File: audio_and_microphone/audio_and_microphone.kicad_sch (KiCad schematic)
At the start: 14 parts, among them U6 ${SIM.PARAMS}

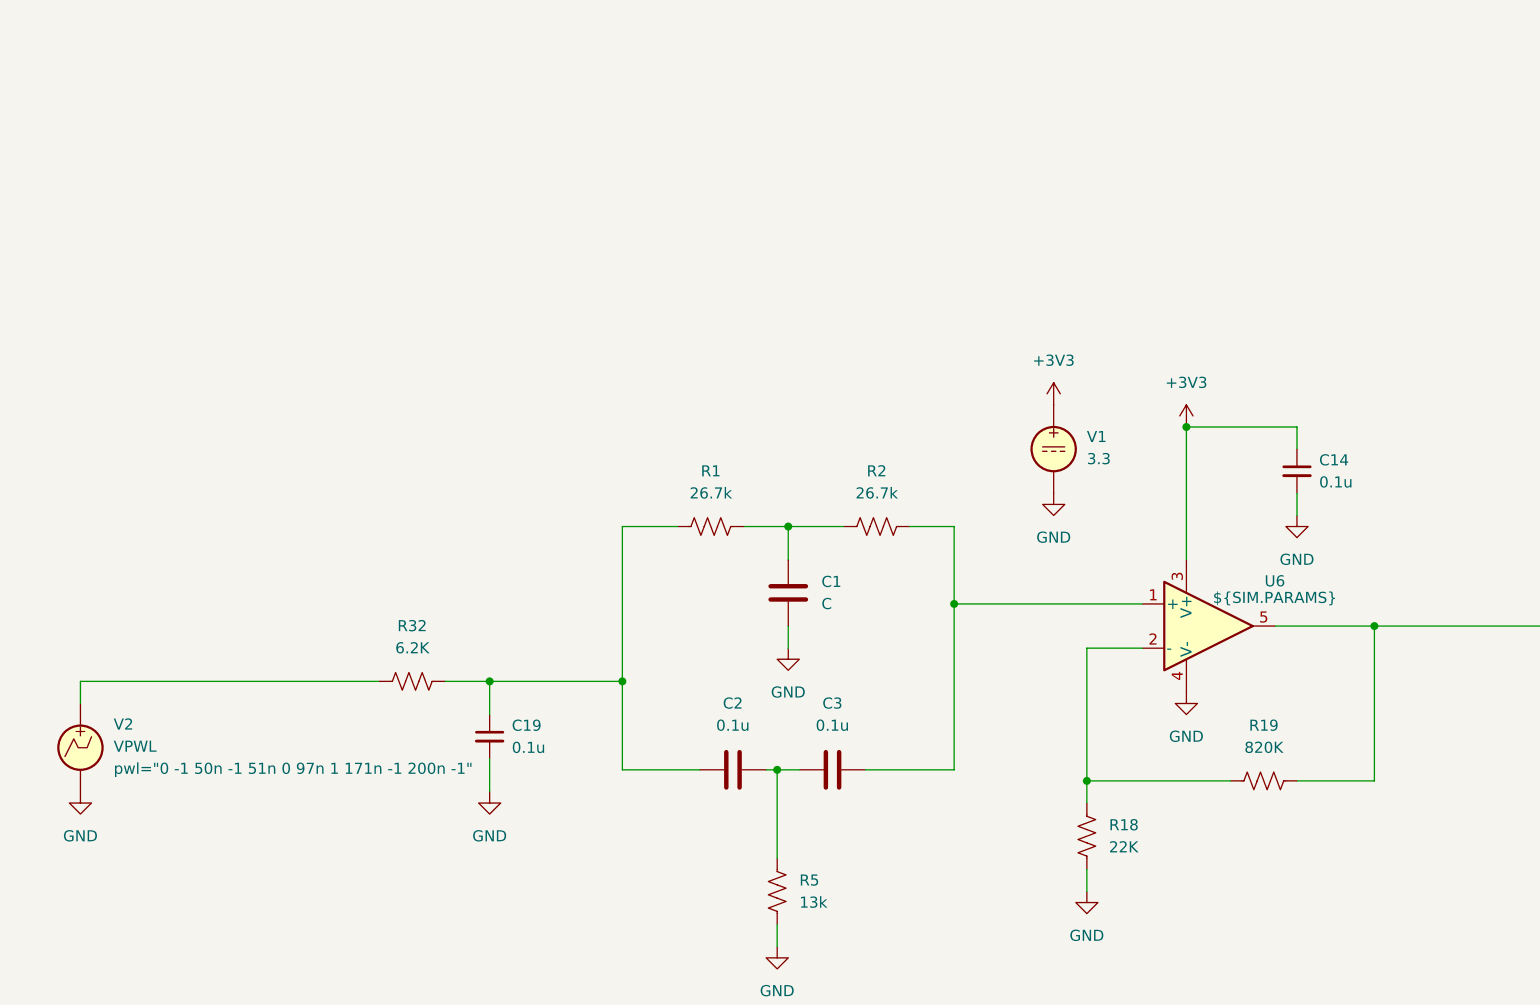
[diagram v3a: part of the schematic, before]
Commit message: pcb update with pin connectors
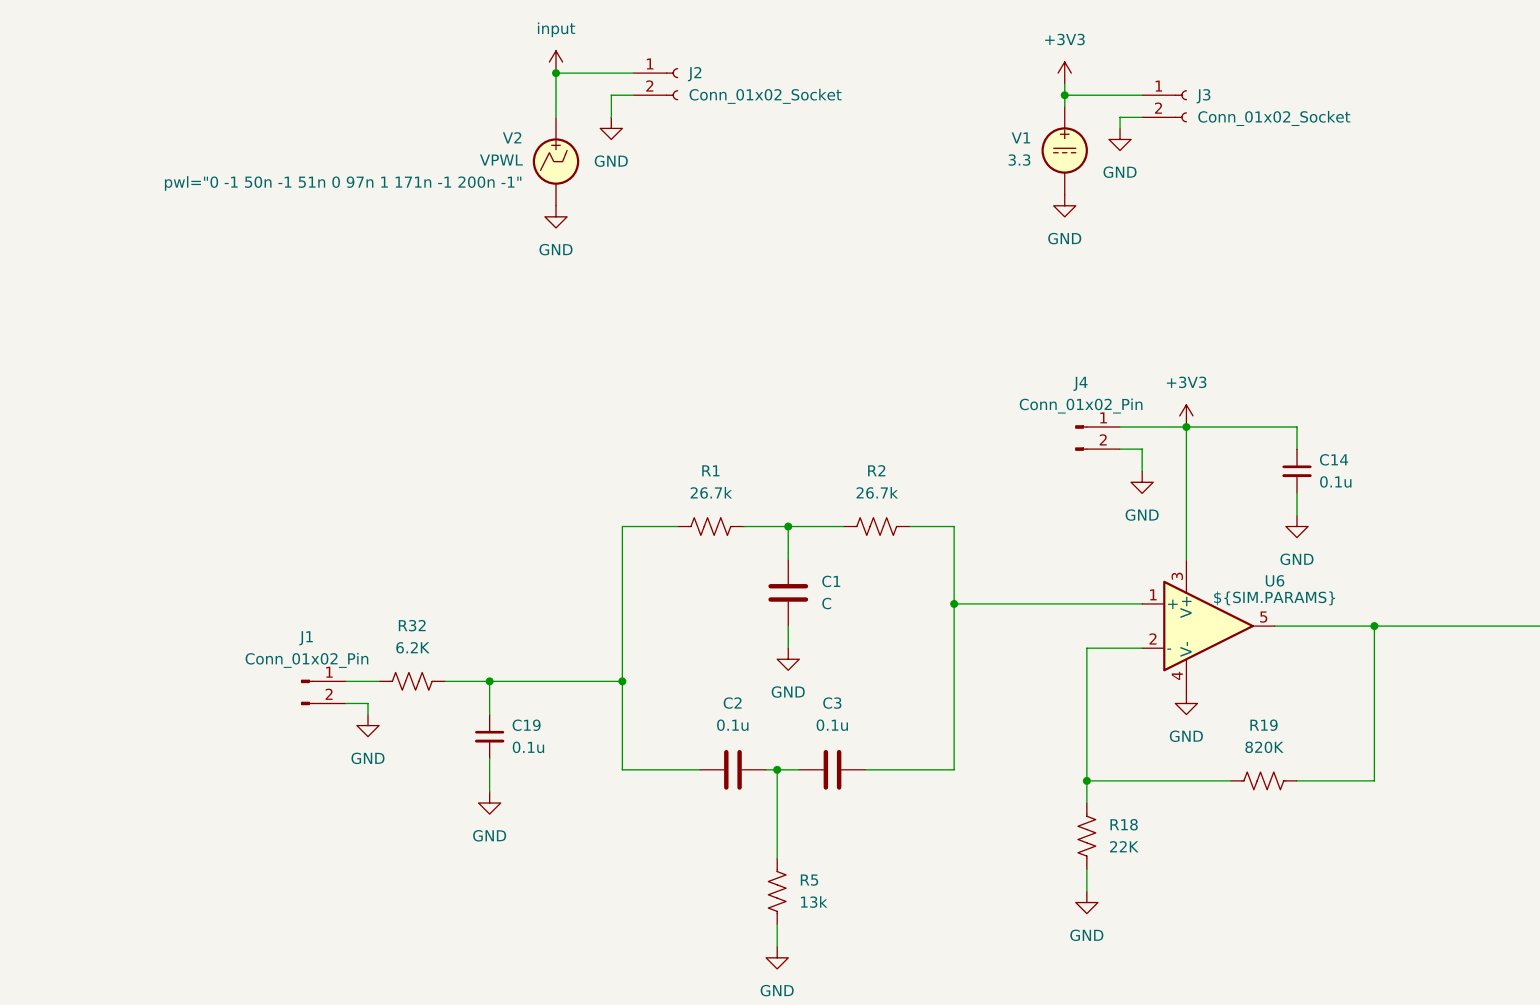
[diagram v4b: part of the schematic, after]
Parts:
- added J1, J4: Conn_01x02_Pin, Connector_JST:JST_XA_B02B-XASK-1-A_1x02_P2.50mm_Vertical, symbol Connector:Conn_01x02_Pin
- added J2, J3: Conn_01x02_Socket, symbol Connector:Conn_01x02_Socket
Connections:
- net +3V3: now also J3.1 (Pin_1), J4.1 (Pin_1)
- net GND: now also J1.2 (Pin_2), J2.2 (Pin_2), J3.2 (Pin_2), J4.2 (Pin_2)
- net at R32.2: now also J1.1 (Pin_1); no longer V2.1
- new net input: J2.1 (Pin_1), V2.1
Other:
- moved on the sheet: V1, V2

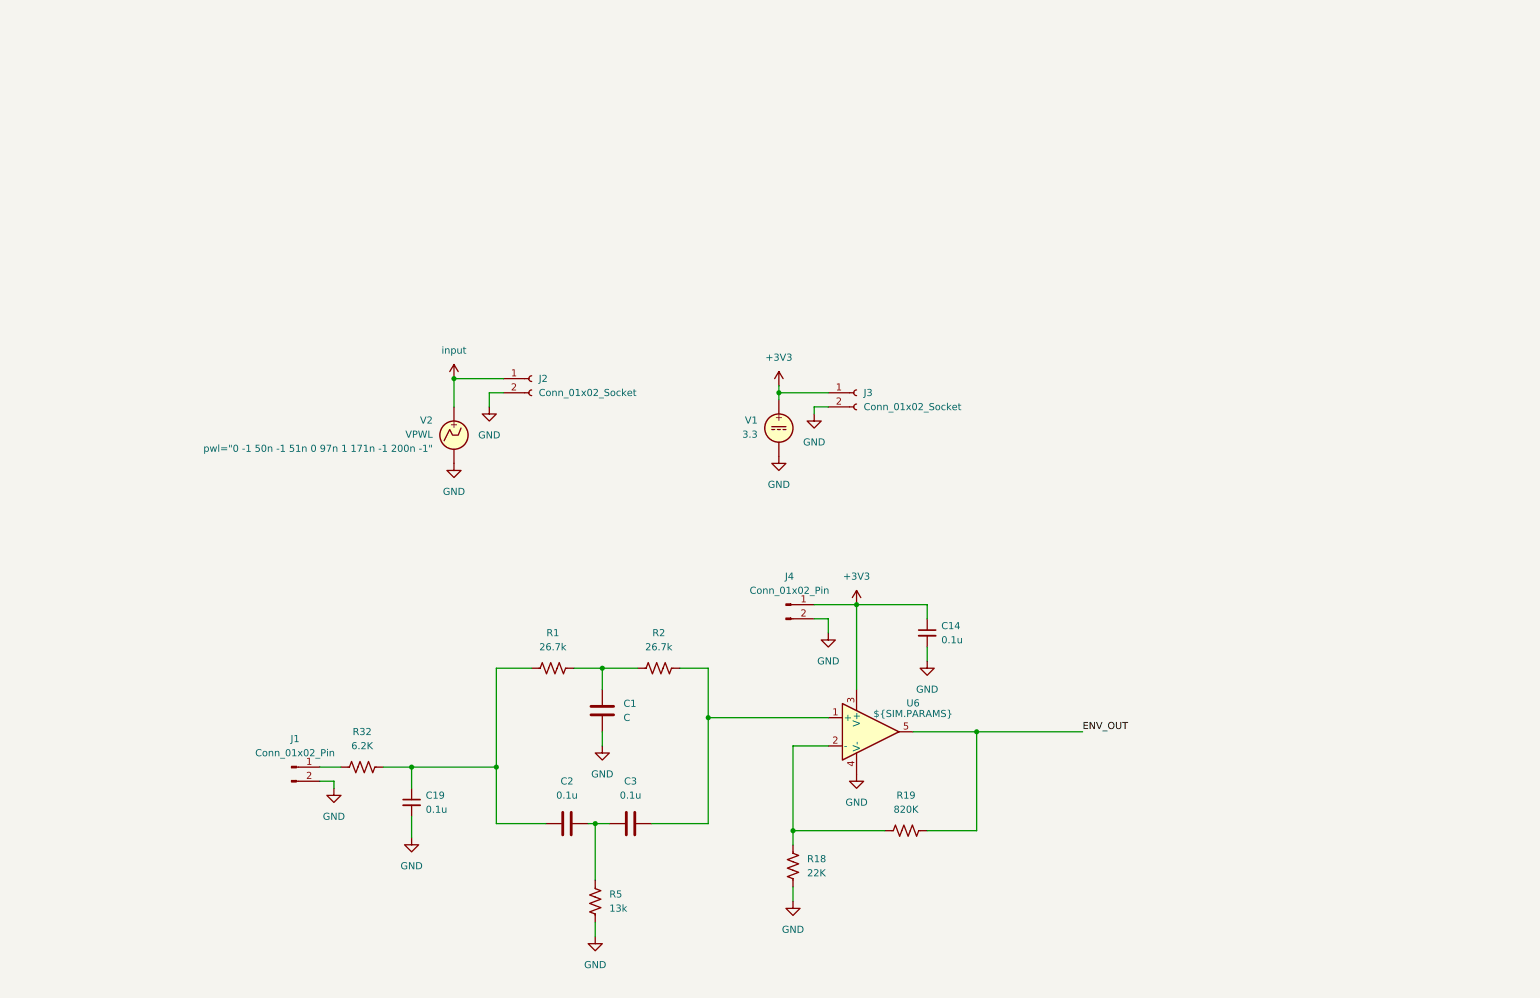
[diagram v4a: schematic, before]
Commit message: pcb with vertical and horizontal male header pins lined up with arduino size
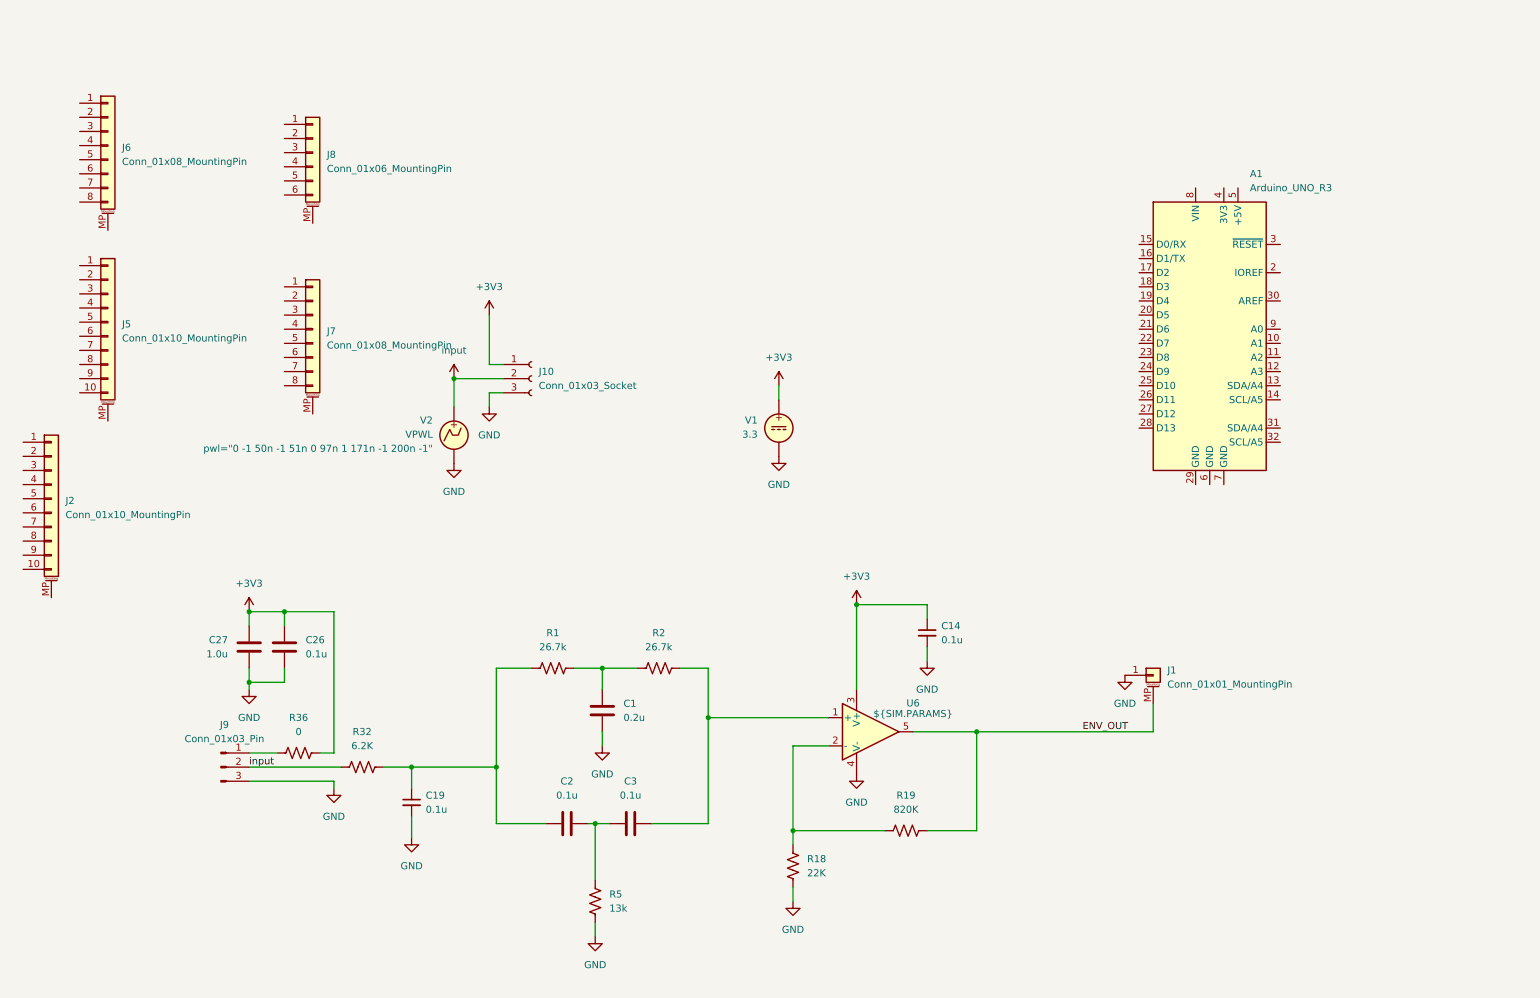
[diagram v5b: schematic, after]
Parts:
- removed J1, J4: Conn_01x02_Pin, Connector_JST:JST_XA_B02B-XASK-1-A_1x02_P2.50mm_Vertical, symbol Connector:Conn_01x02_Pin
- removed J2, J3: Conn_01x02_Socket, symbol Connector:Conn_01x02_Socket
- added A1: Arduino_UNO_R3, Module:Arduino_UNO_R3, symbol MCU_Module:Arduino_UNO_R3
- added C26: 0.1u, Capacitor_SMD:C_0201_0603Metric, symbol Device:C
- added C27: 1.0u, Capacitor_SMD:C_0201_0603Metric, symbol Device:C
- added J1: Conn_01x01_MountingPin, Connector_PinHeader_2.54mm:PinHeader_1x02_P2.54mm_Vertical_SMD_Pin1Left, symbol Connector_Generic_MountingPin:Conn_01x01_MountingPin
- added J10: Conn_01x03_Socket, symbol Connector:Conn_01x03_Socket
- added J2: Conn_01x10_MountingPin, Connector_PinHeader_2.54mm:PinHeader_1x08_P2.54mm_Vertical, symbol Connector_Generic_MountingPin:Conn_01x10_MountingPin
- added J5: Conn_01x10_MountingPin, Connector_PinHeader_2.54mm:PinHeader_1x10_P2.54mm_Vertical_SMD_Pin1Left, symbol Connector_Generic_MountingPin:Conn_01x10_MountingPin
- added J6, J7: Conn_01x08_MountingPin, Connector_PinHeader_2.54mm:PinHeader_1x08_P2.54mm_Vertical_SMD_Pin1Left, symbol Connector_Generic_MountingPin:Conn_01x08_MountingPin
- added J8: Conn_01x06_MountingPin, Connector_PinHeader_2.54mm:PinHeader_1x06_P2.54mm_Vertical_SMD_Pin1Left, symbol Connector_Generic_MountingPin:Conn_01x06_MountingPin
- added J9: Conn_01x03_Pin, Connector_Harwin:Harwin_M20-89003xx_1x03_P2.54mm_Horizontal, symbol Connector:Conn_01x03_Pin
- added R36: 0, Resistor_SMD:R_0201_0603Metric, symbol Device:R_US
- C1: value C -> 0.2u
- V1, V2: now left out of the parts list
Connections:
- net +3V3: now also C26.1, C27.1, J10.1 (Pin_1), R36.1
- net ENV_OUT: now also J1.MP (MountPin)
- net GND: now also C26.2, C27.2, J1.1 (Pin_1), J10.3 (Pin_3), J9.3 (Pin_3)
- net input: now also R32.2, J10.2 (Pin_2), J9.2 (Pin_2)
- new net: J9.1 (Pin_1), R36.2

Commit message: old and new notch filter on schematic and pcb with switch connectors
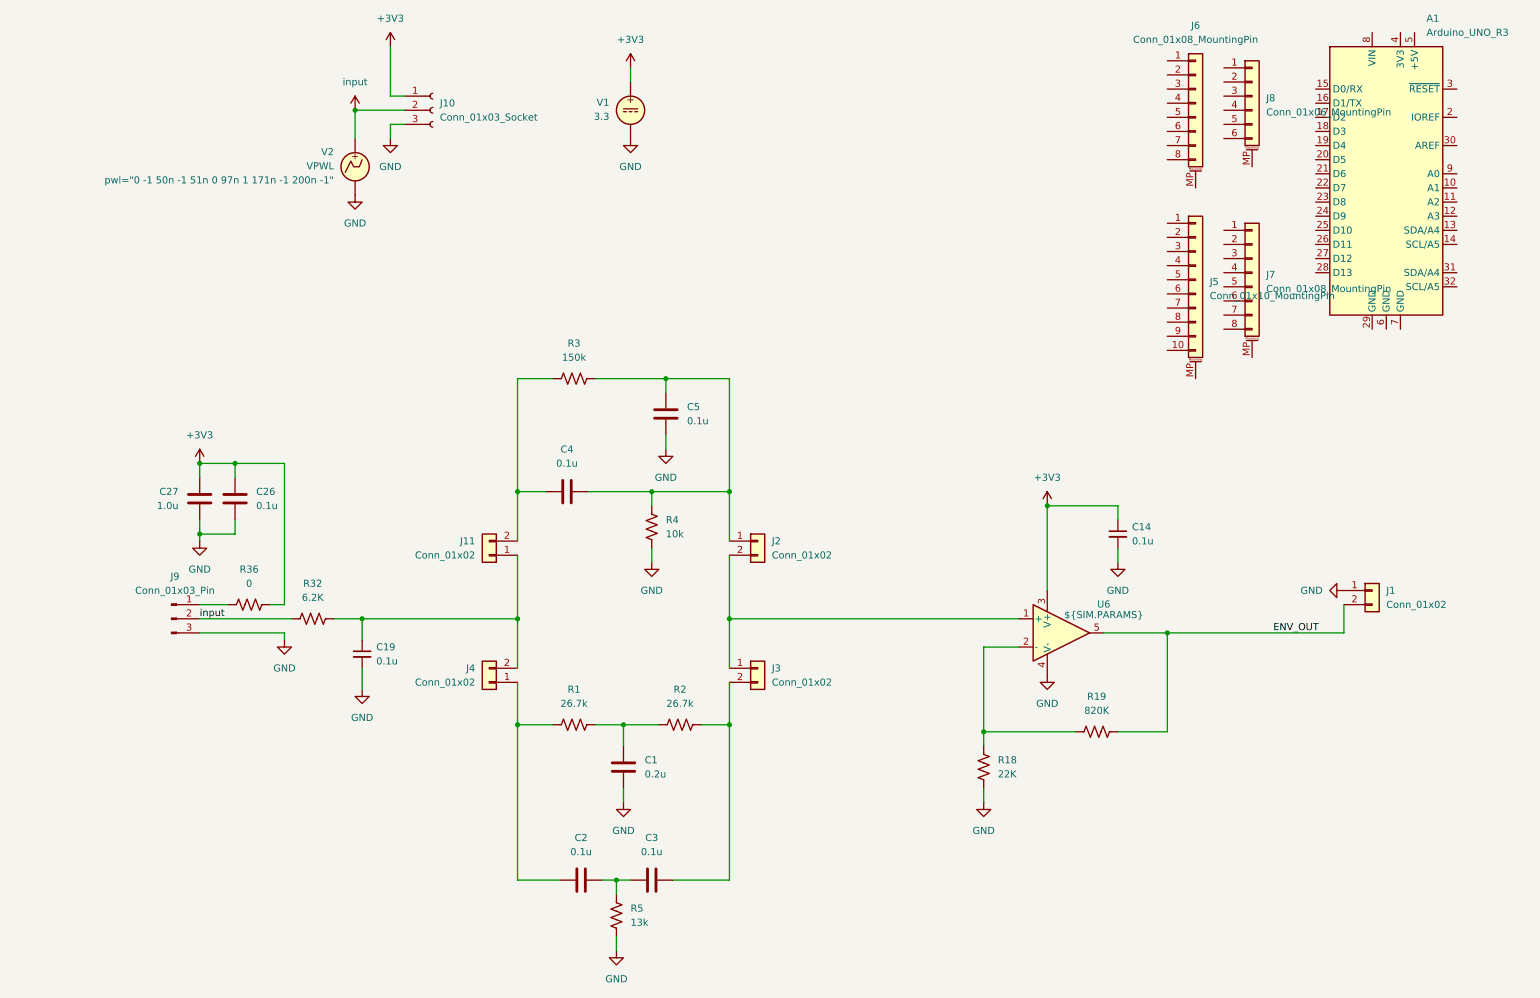
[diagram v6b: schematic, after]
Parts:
- removed J1: Conn_01x01_MountingPin, Connector_PinHeader_2.54mm:PinHeader_1x02_P2.54mm_Vertical_SMD_Pin1Left, symbol Connector_Generic_MountingPin:Conn_01x01_MountingPin
- removed J2: Conn_01x10_MountingPin, Connector_PinHeader_2.54mm:PinHeader_1x08_P2.54mm_Vertical, symbol Connector_Generic_MountingPin:Conn_01x10_MountingPin
- added C4, C5: 0.1u, Capacitor_SMD:C_0201_0603Metric, symbol Device:C
- added J1, J11, J2, J3, J4: Conn_01x02, Connector_PinHeader_2.54mm:PinHeader_1x02_P2.54mm_Vertical, symbol Connector_Generic:Conn_01x02
- added R3: 150k, Resistor_SMD:R_0201_0603Metric, symbol Device:R_US
- added R4: 10k, Resistor_SMD:R_0201_0603Metric, symbol Device:R_US
- J5: footprint Connector_PinHeader_2.54mm:PinHeader_1x10_P2.54mm_Vertical_SMD_Pin1Left -> Connector_PinHeader_2.54mm:PinHeader_1x10_P2.54mm_Vertical
- J6, J7: footprint Connector_PinHeader_2.54mm:PinHeader_1x08_P2.54mm_Vertical_SMD_Pin1Left -> Connector_PinHeader_2.54mm:PinHeader_1x08_P2.54mm_Vertical
- J8: footprint Connector_PinHeader_2.54mm:PinHeader_1x06_P2.54mm_Vertical_SMD_Pin1Left -> Connector_PinHeader_2.54mm:PinHeader_1x06_P2.54mm_Vertical
- J9: footprint Connector_Harwin:Harwin_M20-89003xx_1x03_P2.54mm_Horizontal -> Connector_PinHeader_2.54mm:PinHeader_1x03_P2.54mm_Vertical
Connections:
- net ENV_OUT: now also J1.2 (Pin_2)
- net GND: now also C5.2, J1.1 (Pin_1), R4.2
- net at C2.1, R1.1: now also J4.1 (Pin_1); no longer C19.1, R32.1
- net at C3.2, R2.2: now also J3.2 (Pin_2); no longer U6.1 (+)
- new net: C4.2, C5.1, J2.1 (Pin_1), R3.2, R4.1
- new net: J2.2 (Pin_2), J3.1 (Pin_1), U6.1 (+)
- new net: C19.1, J11.1 (Pin_1), J4.2 (Pin_2), R32.1
- new net: C4.1, J11.2 (Pin_2), R3.1
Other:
- moved on the sheet: A1, C1, C14, C19, C2, C26, C27, C3, J10, J5, J6, J7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
